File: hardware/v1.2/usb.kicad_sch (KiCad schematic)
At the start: 47 parts, among them J3 USB_C_Receptacle_USB2.0_14P, J4 USB_C_Receptacle_USB2.0_14P, J5 USB_C_Receptacle_USB2.0_14P, U1 ECP5U_25F_CABGA256, U6 FT231XQ, U7 TPD2EUSB30A, U8 TPD2EUSB30A, U9 TPD2EUSB30A

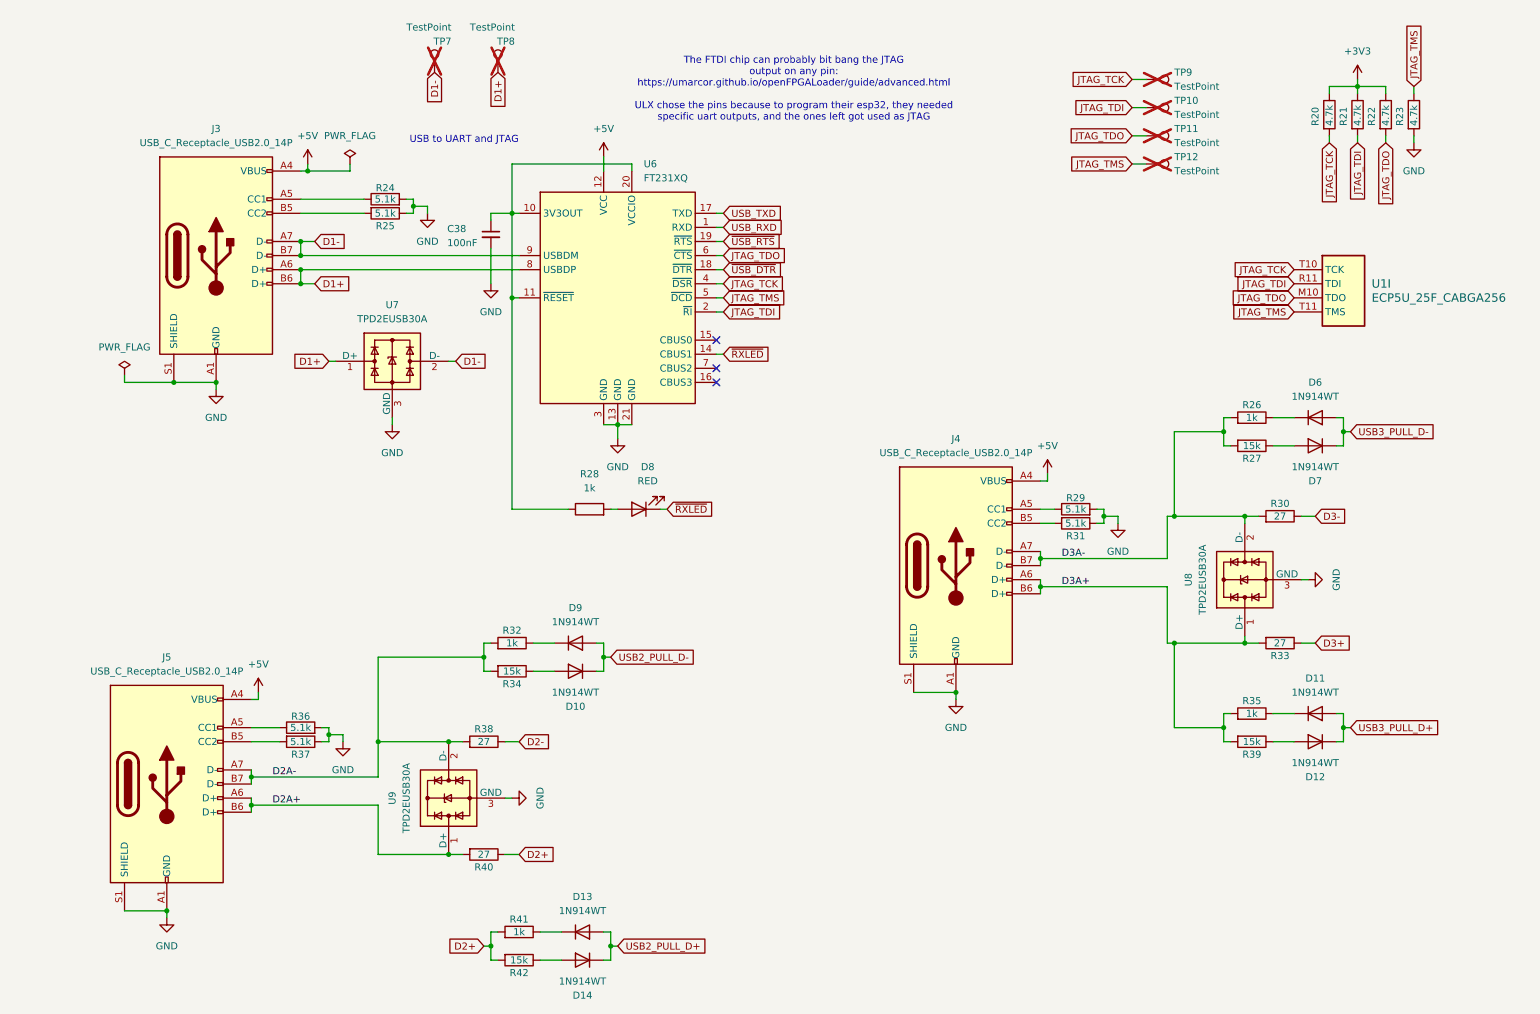
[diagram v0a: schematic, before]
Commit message: Custom ECP5-CABGA256 symbol
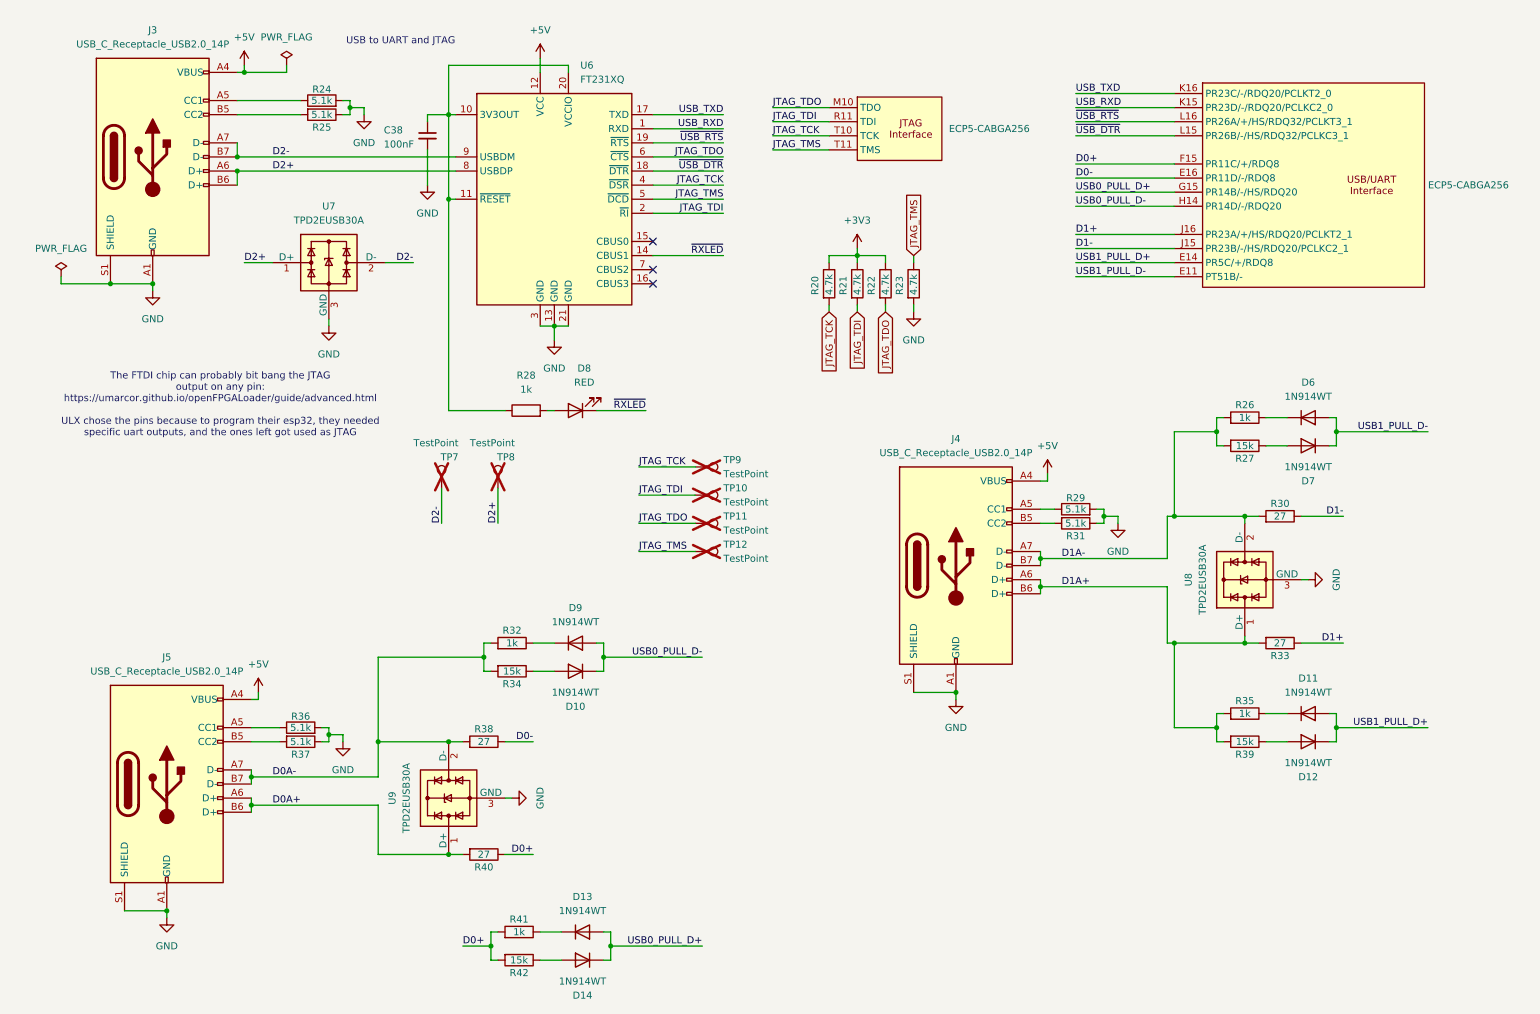
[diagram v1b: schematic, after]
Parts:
- removed U1: ECP5U_25F_CABGA256, Package_BGA:BGA-256_14.0x14.0mm_Layout16x16_P0.8mm_Ball0.45mm_Pad0.32mm_NSMD, symbol josh:ECP5U_12_CABGA256
- added U1: ECP5-CABGA256, Package_BGA:BGA-256_14.0x14.0mm_Layout16x16_P0.8mm_Ball0.45mm_Pad0.32mm_NSMD, symbol icepi-lib:LFE5U-25F-6BG256x
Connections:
- net D3+ is gone; now on net D1+: R33.1
- net D3- is gone; now on net D1-: R30.1
- net D1+: now also U1.J16 (PR23A/+/HS/RDQ20/PCLKT2_1); no longer J3.A6 (D+), J3.B6 (D+), TP8.1, U6.8 (USBDP), U7.1 (D+)
- net D1-: now also U1.J15 (PR23B/-/HS/RDQ20/PCLKC2_1); no longer J3.A7 (D-), J3.B7 (D-), TP7.1, U6.9 (USBDM), U7.2 (D-)
- net D2+: now also J3.A6 (D+), J3.B6 (D+), TP8.1, U6.8 (USBDP), U7.1 (D+); no longer R40.1, R41.2, R42.2
- net D2-: now also J3.A7 (D-), J3.B7 (D-), TP7.1, U6.9 (USBDM), U7.2 (D-); no longer R38.1
- net JTAG_TCK: now also U1.T10 (TCK)
- net JTAG_TDI: now also U1.R11 (TDI)
- net JTAG_TDO: now also U1.M10 (TDO)
- net JTAG_TMS: now also U1.T11 (TMS)
- net USB_RXD: now also U1.K15 (PR23D/-/RDQ20/PCLKC2_0)
- net USB_TXD: now also U1.K16 (PR23C/-/RDQ20/PCLKT2_0)
- net ~{USB_DTR}: now also U1.L15 (PR26B/-/HS/RDQ32/PCLKC3_1)
- net ~{USB_RTS}: now also U1.L16 (PR26A/+/HS/RDQ32/PCLKT3_1)
- net D2A+ renamed D0A+
- net D2A- renamed D0A-
- net D3A+ renamed D1A+
- net D3A- renamed D1A-
- net USB2_PULL_D+ renamed USB0_PULL_D+
- net USB0_PULL_D+: now also U1.G15 (PR14B/-/HS/RDQ20)
- net USB2_PULL_D- renamed USB0_PULL_D-
- net USB0_PULL_D-: now also U1.H14 (PR14D/-/RDQ20)
- net USB3_PULL_D+ renamed USB1_PULL_D+
- net USB1_PULL_D+: now also U1.E14 (PR5C/+/RDQ8)
- net USB3_PULL_D- renamed USB1_PULL_D-
- net USB1_PULL_D-: now also U1.E11 (PT51B/-)
- new net D0+: R40.1, R41.2, R42.2, U1.F15 (PR11C/+/RDQ8)
- new net D0-: R38.1, U1.E16 (PR11D/-/RDQ8)
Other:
- moved on the sheet: C38, D11, D12, D6, D7, D8, J3, R20, R21, R22, R23, R24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

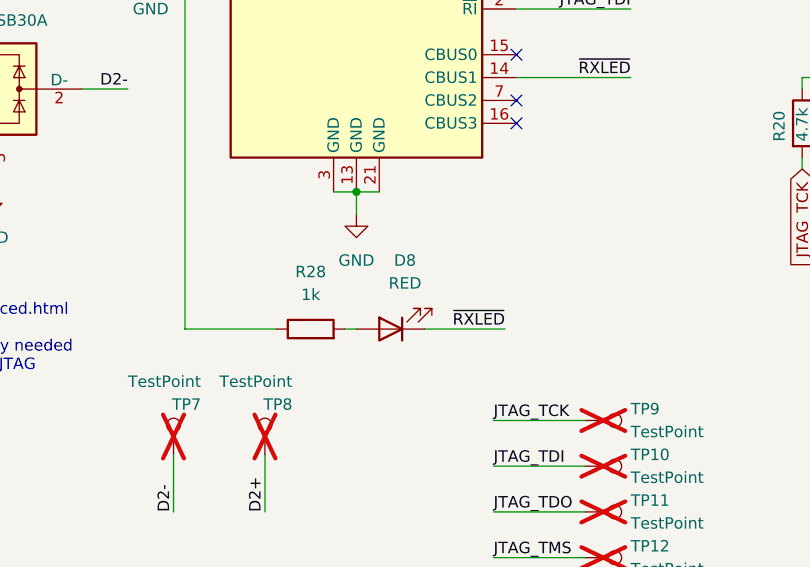
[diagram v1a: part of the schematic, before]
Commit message: Put better pin names for LPF files
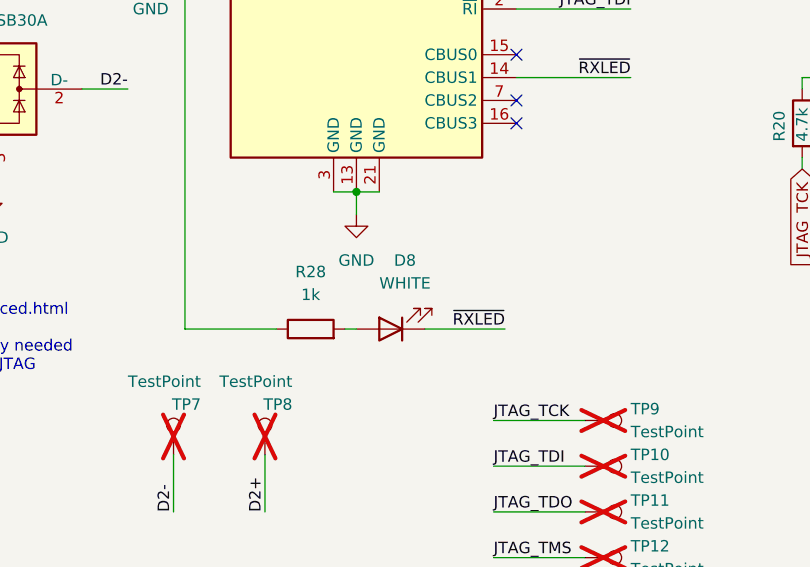
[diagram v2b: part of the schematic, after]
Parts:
- D8: value RED -> WHITE; LCSC Part # C2286 -> C2290
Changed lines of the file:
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@@
 			)
 		)
-		(property "Value" "RED"
+		(property "Value" "WHITE"
 			(at 114.6175 83.82 0)
 			(effects
@@
 			)
 		)
-		(property "LCSC Part #" "C2286 "
+		(property "LCSC Part #" "C2290"
 			(at 113.03 88.9 0)
 			(effects

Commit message: Don't overwrite v1.2 with v1.3
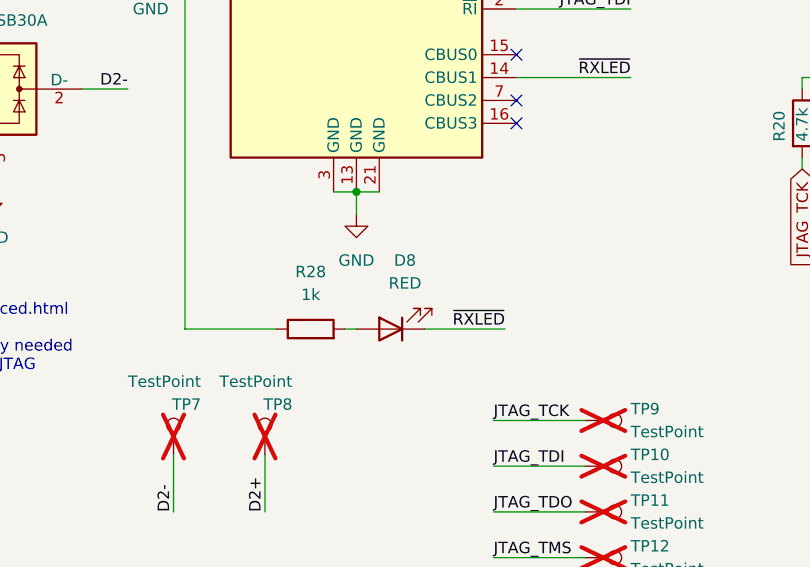
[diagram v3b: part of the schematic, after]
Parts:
- D8: value WHITE -> RED; LCSC Part # C2290 -> C2286
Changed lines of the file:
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@@
 			)
 		)
-		(property "Value" "WHITE"
+		(property "Value" "RED"
 			(at 114.6175 83.82 0)
 			(effects
@@
 			)
 		)
-		(property "LCSC Part #" "C2290"
+		(property "LCSC Part #" "C2286 "
 			(at 113.03 88.9 0)
 			(effects

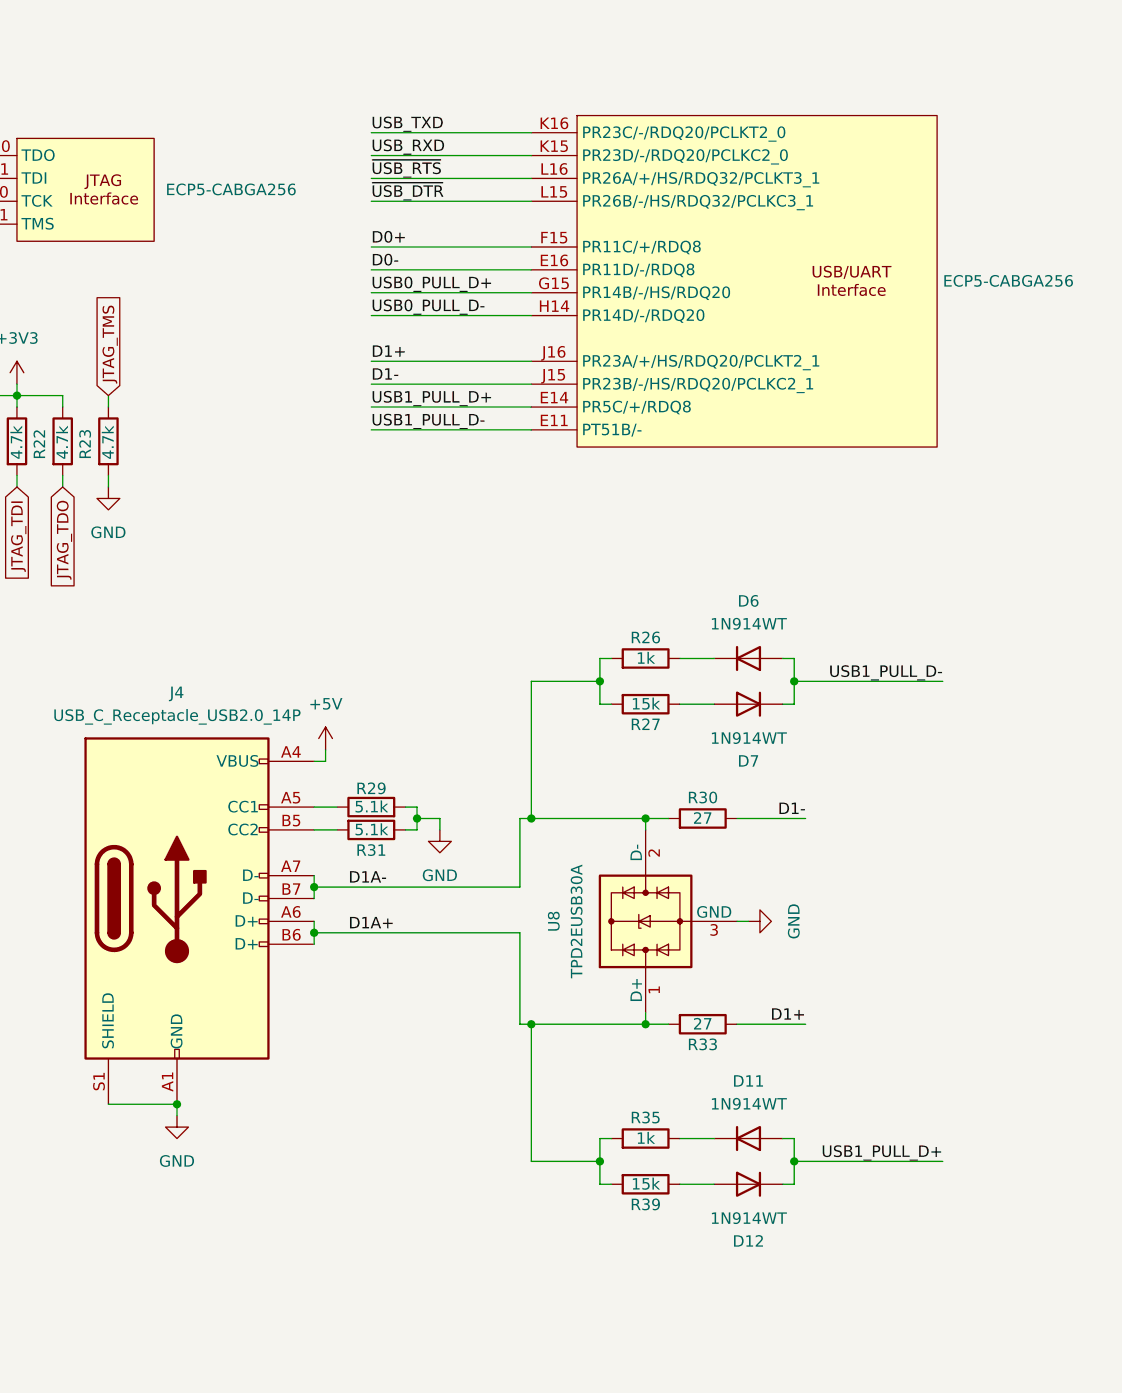
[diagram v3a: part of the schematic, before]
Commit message: UART to PS2 converter
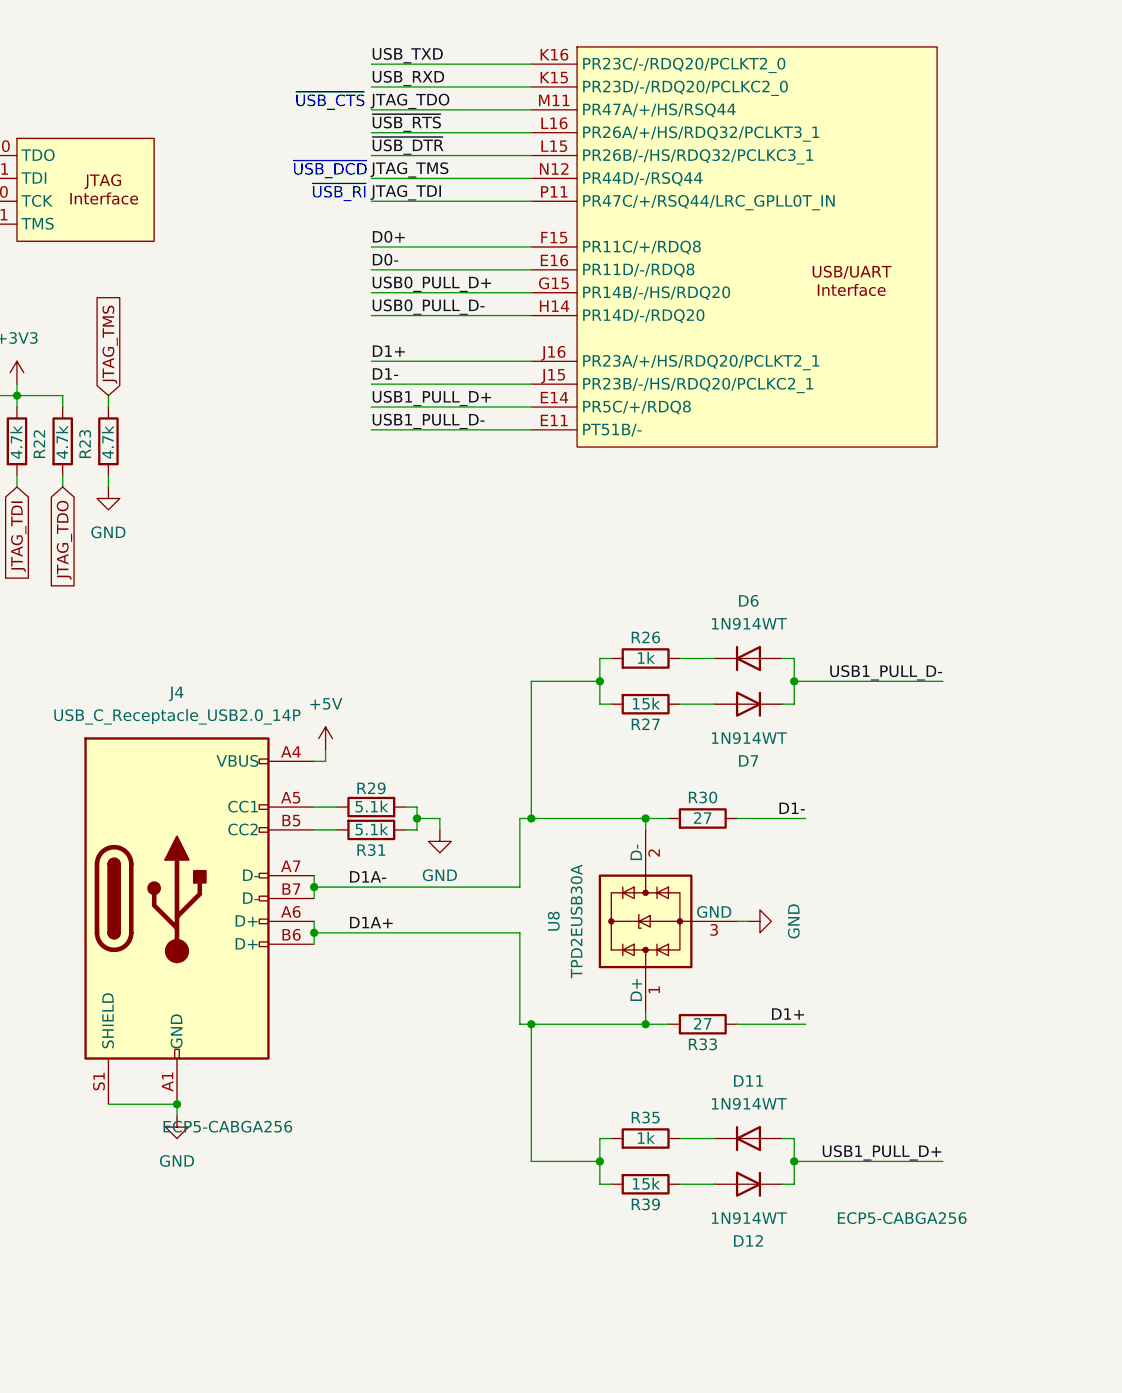
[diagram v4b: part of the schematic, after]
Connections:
- net JTAG_TDI: now also U1.P11 (PR47C/+/RSQ44/LRC_GPLL0T_IN)
- net JTAG_TDO: now also U1.M11 (PR47A/+/HS/RSQ44)
- net JTAG_TMS: now also U1.N12 (PR44D/-/RSQ44)
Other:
- note added: "~{USB_CTS}"
- note added: "~{USB_DCD}"
- note added: "~{USB_RI}"
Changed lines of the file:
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@@
 		(comment 9 "OSHWA FR000026")
 	)
+	(text "~{USB_DCD}"
+		(exclude_from_sim no)
+		(at 198.628 36.068 0)
+		(effects
+			(font
+				(size 1.27 1.27)
+			)
+		)
+	)
+	(text "~{USB_RI}"
+		(exclude_from_sim no)
+		(at 199.644 38.608 0)
+		(effects
+			(font
+				(size 1.27 1.27)
+			)
+		)
+	)
 	(text "USB to UART and JTAG"
 		(exclude_from_sim no)
@@
 		)
 	)
+	(text "~{USB_CTS}"
+		(exclude_from_sim no)
+		(at 198.628 28.448 0)
+		(effects
+			(font
+				(size 1.27 1.27)
+			)
+		)
+	)
 	(junction
 		(at 77.47 148.59)
@@
 	(wire
 		(pts
-			(xy 203.2 39.37) (xy 220.98 39.37)
+			(xy 203.2 34.29) (xy 220.98 34.29)
 		)
 		(stroke
@@
 	(wire
 		(pts
-			(xy 203.2 31.75) (xy 220.98 31.75)
+			(xy 203.2 24.13) (xy 220.98 24.13)
 		)
 		(stroke
@@
 	(wire
 		(pts
-			(xy 203.2 34.29) (xy 220.98 34.29)
+			(xy 203.2 26.67) (xy 220.98 26.67)
 		)
 		(stroke
@@
 	(wire
 		(pts
+			(xy 203.2 29.21) (xy 220.98 29.21)
+		)
+		(stroke
+			(width 0)
+			(type default)
+		)
+	)
+	(wire
+		(pts
 			(xy 90.17 50.8) (xy 90.17 35.56)
 		)
@@
 	(wire
 		(pts
+			(xy 203.2 36.83) (xy 220.98 36.83)
+		)
+		(stroke
+			(width 0)
+			(type default)
+		)
+	)
+	(wire
+		(pts
+			(xy 203.2 39.37) (xy 220.98 39.37)
+		)
+		(stroke
+			(width 0)
+			(type default)
+		)
+	)
+	(wire
+		(pts
 			(xy 237.49 90.17) (xy 241.3 90.17)
 		)
@@
 	(wire
 		(pts
-			(xy 203.2 36.83) (xy 220.98 36.83)
+			(xy 203.2 31.75) (xy 220.98 31.75)
 		)
 		(stroke
@@
 	)
 	(label "~{USB_RTS}"
-		(at 203.2 36.83 0)
+		(at 203.2 31.75 0)
 		(effects
 			(font
@@
 		)
 	)
+	(label "JTAG_TDI"
+		(at 203.2 39.37 0)
+		(effects
+			(font
+				(size 1.27 1.27)
+			)
+			(justify left bottom)
+		)
+	)
 	(label "D2-"
 		(at 88.9 109.22 90)
@@
 	)
 	(label "USB_TXD"
-		(at 203.2 31.75 0)
+		(at 203.2 24.13 0)
 		(effects
 			(font
@@
 	)
 	(label "~{USB_DTR}"
-		(at 203.2 39.37 0)
+		(at 203.2 34.29 0)
 		(effects
 			(font
@@
 		)
 	)
+	(label "JTAG_TMS"
+		(at 203.2 36.83 0)
+		(effects
+			(font
+				(size 1.27 1.27)
+			)
+			(justify left bottom)
+		)
+	)
 	(label "USB_RXD"
 		(at 139.7 38.1 180)
@@
 		)
 	)
+	(label "JTAG_TDO"
+		(at 203.2 29.21 0)
+		(effects
+			(font
+				(size 1.27 1.27)
+			)
+			(justify left bottom)
+		)
+	)
 	(label "JTAG_TCK"
 		(at 148.59 39.37 0)
@@
 	)
 	(label "USB_RXD"
-		(at 203.2 34.29 0)
+		(at 203.2 26.67 0)
 		(effects
 			(font
@@
 	)
 	(symbol
+		(lib_name "LFE5U-25F-6BG256x_1")
 		(lib_id "icepi-lib:LFE5U-25F-6BG256x")
 		(at 171.45 38.1 0)
@@
 		)
 		(property "Value" "ECP5-CABGA256"
-			(at 180.34 38.1 0)
+			(at 179.9433 142.24 0)
 			(effects
 				(font
@@
 		)
 		(instances
-			(project "icepi-zero"
+			(project ""
+				(path "/f88da08e-cf42-4d03-a08f-3f602fe6658d/17c9c9b3-f379-4e1f-a876-d3fcf0529a4d"
+					(reference "U1")
+					(unit 2)
+				)
 				(path "/f88da08e-cf42-4d03-a08f-3f602fe6658d/b8c813e2-b0ac-42df-b4a2-893985a7d29c"
 					(reference "U1")
@@
 		)
 		(property "Value" "ECP5-CABGA256"
-			(at 266.7 48.26 0)
+			(at 254.8733 152.4 0)
 			(effects
 				(font
@@
 		(pin "F8"
 		)
+		(pin "P11"
+		)
 		(instances
-			(project "icepi-zero"
+			(project ""
+				(path "/f88da08e-cf42-4d03-a08f-3f602fe6658d/17c9c9b3-f379-4e1f-a876-d3fcf0529a4d"
+					(reference "U1")
+					(unit 5)
+				)
 				(path "/f88da08e-cf42-4d03-a08f-3f602fe6658d/b8c813e2-b0ac-42df-b4a2-893985a7d29c"
 					(reference "U1")
